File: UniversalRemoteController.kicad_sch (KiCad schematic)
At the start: 0 parts

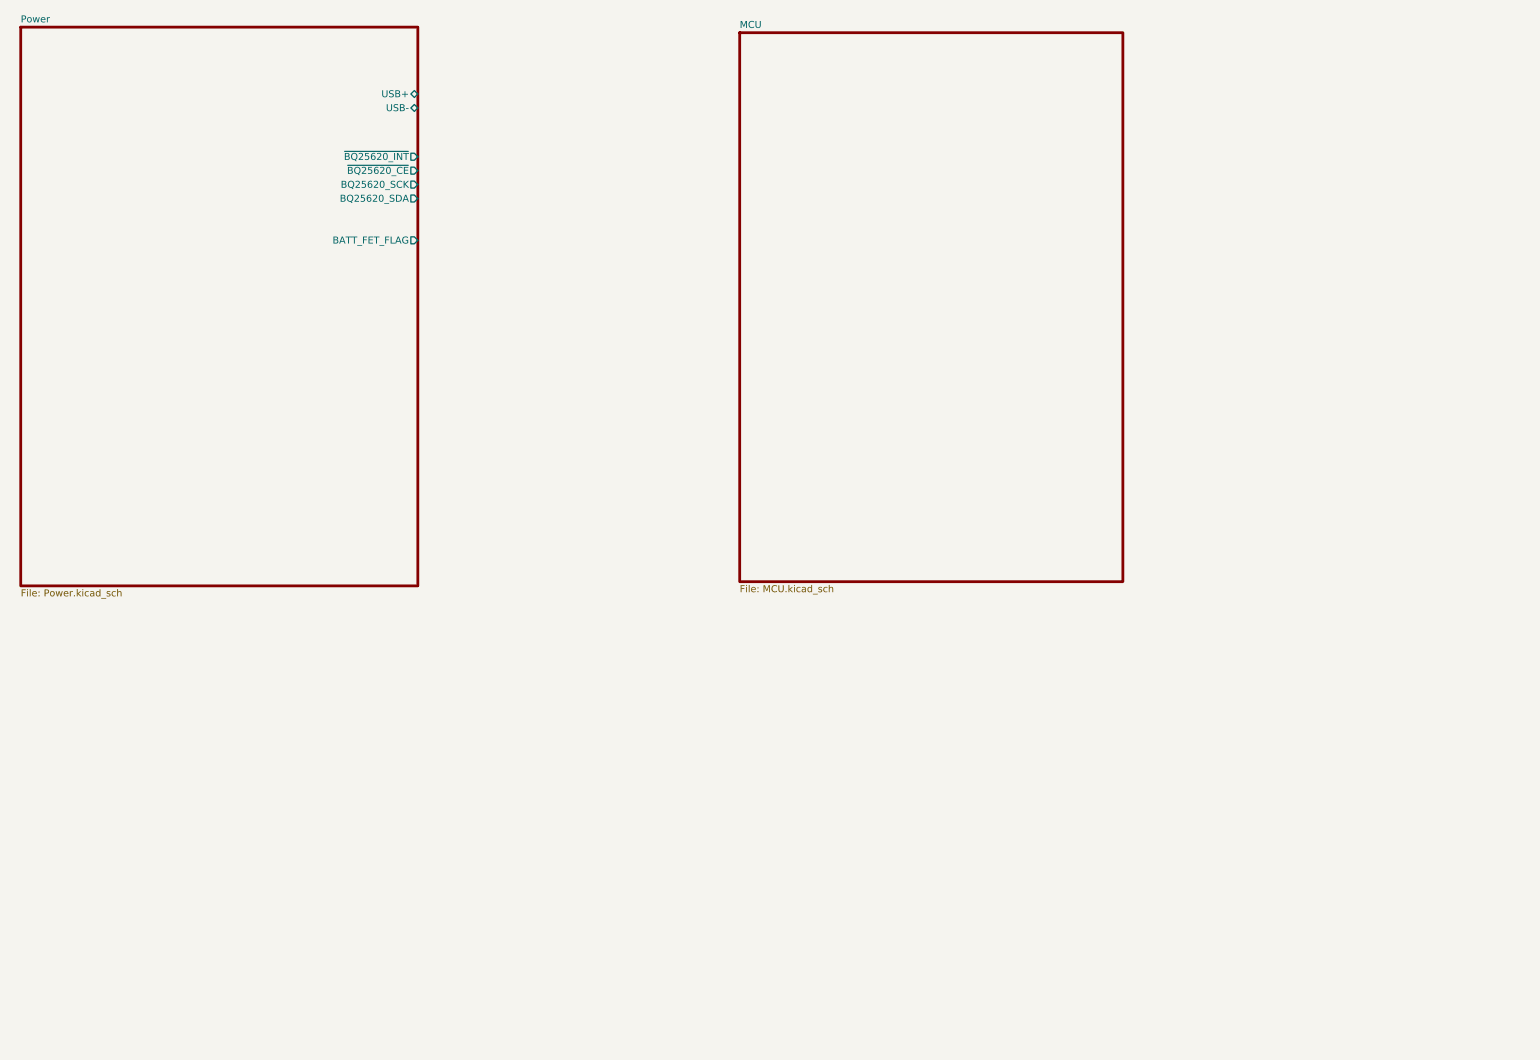
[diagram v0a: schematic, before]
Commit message: Add the SDRAM ic
16MB SDRAM add
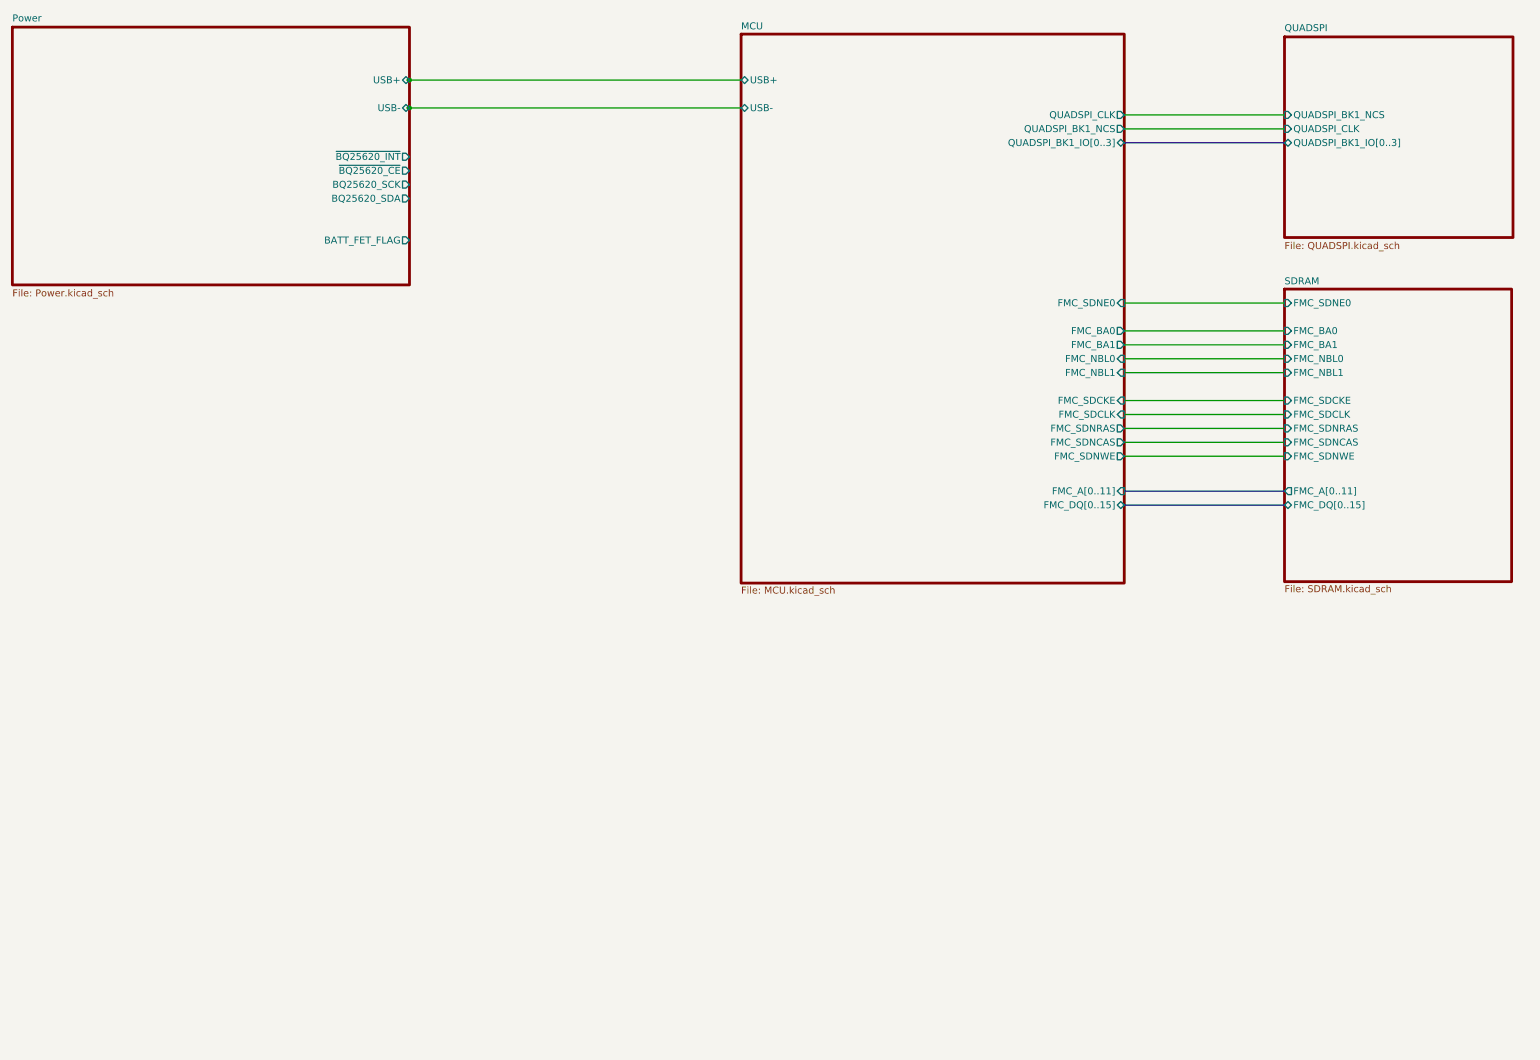
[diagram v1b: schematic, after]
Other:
- added sheet QUADSPI (QUADSPI.kicad_sch)
- added sheet SDRAM (SDRAM.kicad_sch)
- sheet MCU ports: added FMC_A[0..11], FMC_BA0, FMC_BA1, FMC_DQ[0..15], FMC_NBL0, FMC_NBL1, FMC_SDCKE, FMC_SDCLK, FMC_SDNCAS, FMC_SDNE0, FMC_SDNRAS, FMC_SDNWE, QUADSPI_BK1_IO[0..3], QUADSPI_BK1_NCS, QUADSPI_CLK, USB+, USB-; removed none

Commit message: Add the nrf and joystic module
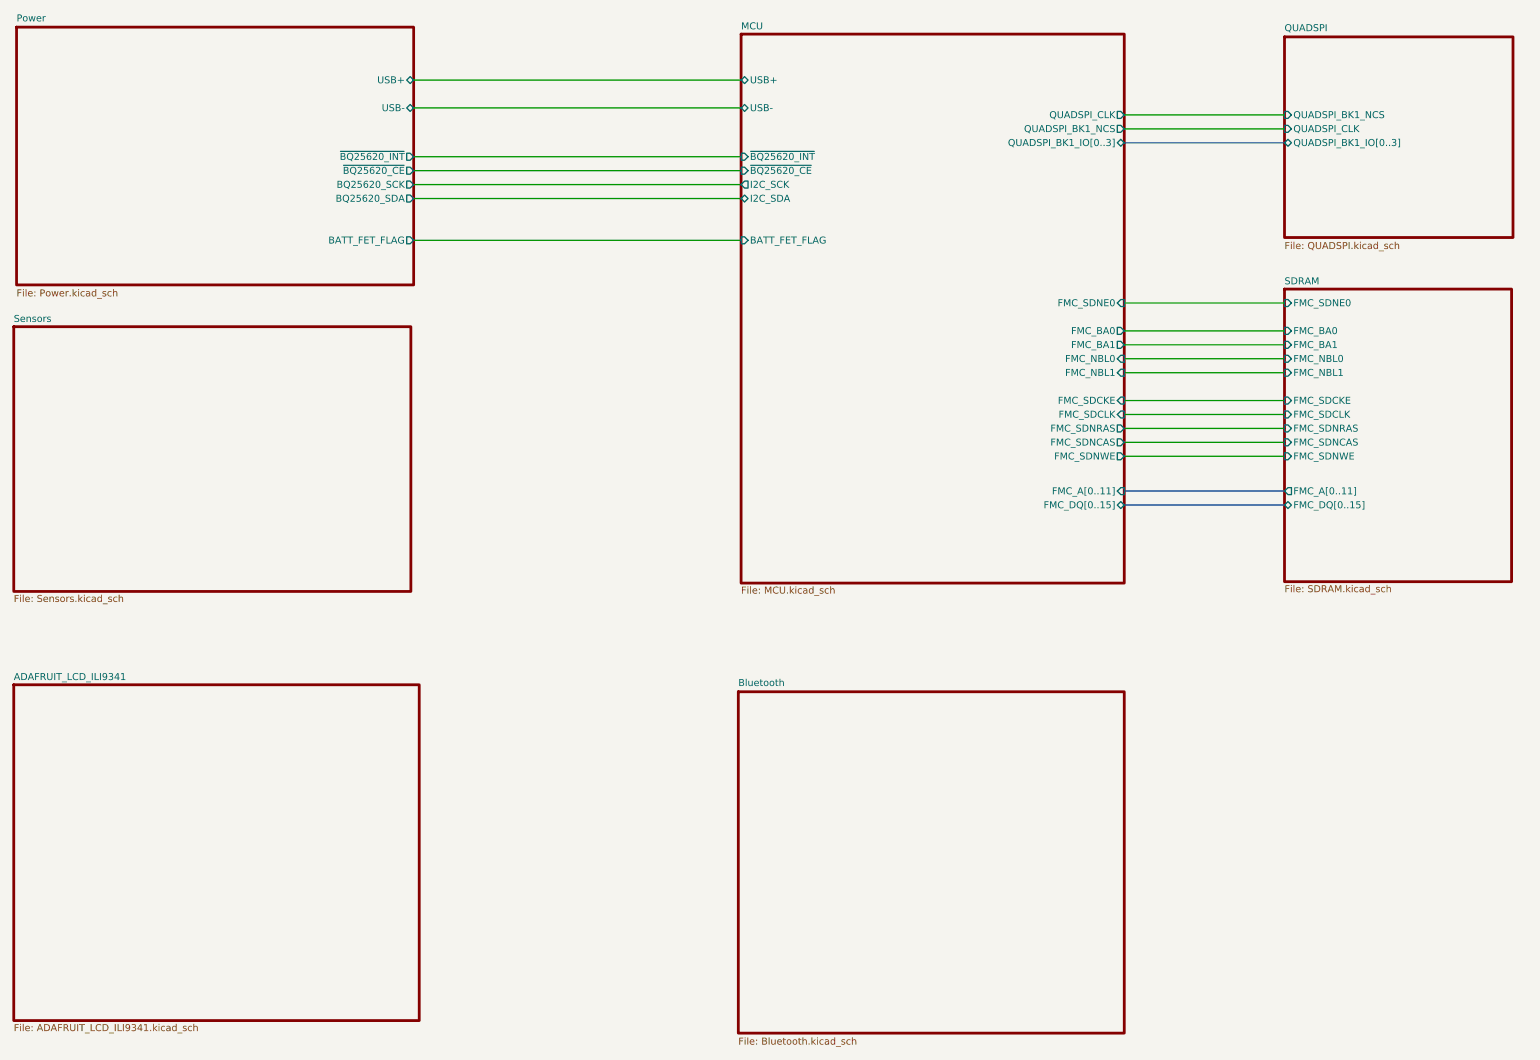
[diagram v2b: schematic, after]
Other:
- added sheet ADAFRUIT_LCD_ILI9341 (ADAFRUIT_LCD_ILI9341.kicad_sch)
- added sheet Bluetooth (Bluetooth.kicad_sch)
- added sheet Sensors (Sensors.kicad_sch)
- sheet MCU ports: added BATT_FET_FLAG, I2C_SCK, I2C_SDA, ~{BQ25620_CE}, ~{BQ25620_INT}; removed none
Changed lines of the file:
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@@
 		(rev "1.0")
 	)
-	(junction
-		(at 124.968 48.26)
-		(diameter 0)
-		(color 0 0 0 0)
-	)
-	(junction
-		(at 124.968 43.18)
-		(diameter 0)
-		(color 0 0 0 0)
+	(wire
+		(pts
+			(xy 125.73 72.39) (xy 185.42 72.39)
+		)
+		(stroke
+			(width 0)
+			(type default)
+		)
 	)
 	(wire
@@
 	(wire
 		(pts
-			(xy 124.968 48.26) (xy 185.42 48.26)
+			(xy 125.73 48.26) (xy 185.42 48.26)
 		)
 		(stroke
@@
 	(wire
 		(pts
-			(xy 124.968 43.18) (xy 185.42 43.18)
+			(xy 125.73 62.23) (xy 185.42 62.23)
+		)
+		(stroke
+			(width 0)
+			(type default)
+		)
+	)
+	(wire
+		(pts
+			(xy 125.73 43.18) (xy 185.42 43.18)
 		)
 		(stroke
@@
 	(wire
 		(pts
+			(xy 125.73 64.77) (xy 185.42 64.77)
+		)
+		(stroke
+			(width 0)
+			(type default)
+		)
+	)
+	(wire
+		(pts
 			(xy 255.27 109.22) (xy 284.48 109.22)
 		)
@@
 		)
 	)
-	(wire
-		(pts
-			(xy 124.46 43.18) (xy 124.968 43.18)
-		)
-		(stroke
-			(width 0)
-			(type default)
-		)
-	)
-	(wire
-		(pts
-			(xy 124.46 48.26) (xy 124.968 48.26)
-		)
-		(stroke
-			(width 0)
-			(type default)
-		)
-	)
 	(bus
 		(pts
@@
 	(wire
 		(pts
+			(xy 125.73 59.69) (xy 185.42 59.69)
+		)
+		(stroke
+			(width 0)
+			(type default)
+		)
+	)
+	(wire
+		(pts
 			(xy 255.27 106.68) (xy 284.48 106.68)
 		)
@@
 		(pts
 			(xy 255.27 111.76) (xy 284.48 111.76)
+		)
+		(stroke
+			(width 0)
+			(type default)
+		)
+	)
+	(wire
+		(pts
+			(xy 125.73 57.15) (xy 185.42 57.15)
 		)
 		(stroke
@@
 	)
 	(sheet
+		(at 52.832 153.416)
+		(size 73.914 61.214)
+		(fields_autoplaced yes)
+		(stroke
+			(width 0.508)
+			(type solid)
+			(color 255 163 155 1)
+		)
+		(fill
+			(color 254 255 106 1.0000)
+		)
+		(property "Sheetname" "ADAFRUIT_LCD_ILI9341"
+			(at 52.832 152.7044 0)
+			(effects
+				(font
+					(size 1.27 1.27)
+				)
+				(justify left bottom)
+			)
+		)
+		(property "Sheetfile" "ADAFRUIT_LCD_ILI9341.kicad_sch"
+			(at 52.832 215.2146 0)
+			(effects
+				(font
+					(size 1.27 1.27)
+				)
+				(justify left top)
+			)
+		)
+		(instances
+			(project "UniversalRemoteController"
+				(path "/dfe540b7-7587-4b82-94ea-0a8290455e48"
+					(page "7")
+				)
+			)
+		)
+	)
+	(sheet
 		(at 185.42 34.798)
 		(size 69.85 100.076)
@@
 				)
 				(justify right)
+			)
+		)
+		(pin "I2C_SCK" output
+			(at 185.42 62.23 180)
+			(effects
+				(font
+					(size 1.27 1.27)
+				)
+				(justify left)
+			)
+		)
+		(pin "I2C_SDA" bidirectional
+			(at 185.42 64.77 180)
+			(effects
+				(font
+					(size 1.27 1.27)
+				)
+				(justify left)
+			)
+		)
+		(pin "~{BQ25620_INT}" input
+			(at 185.42 57.15 180)
+			(effects
+				(font
+					(size 1.27 1.27)
+				)
+				(justify left)
+			)
+		)
+		(pin "BATT_FET_FLAG" input
+			(at 185.42 72.39 180)
+			(effects
+				(font
+					(size 1.27 1.27)
+				)
+				(justify left)
+			)
+		)
+		(pin "~{BQ25620_CE}" input
+			(at 185.42 59.69 180)
+			(effects
+				(font
+					(size 1.27 1.27)
+				)
+				(justify left)
 			)
 		)
@@
 	)
 	(sheet
-		(at 52.578 33.528)
-		(size 72.39 46.99)
+		(at 52.832 88.138)
+		(size 72.39 48.26)
 		(fields_autoplaced yes)
 		(stroke
@@
 			(color 254 255 106 1.0000)
 		)
+		(property "Sheetname" "Sensors"
+			(at 52.832 87.4264 0)
+			(effects
+				(font
+					(size 1.27 1.27)
+				)
+				(justify left bottom)
+			)
+		)
+		(property "Sheetfile" "Sensors.kicad_sch"
+			(at 52.832 136.9826 0)
+			(effects
+				(font
+					(size 1.27 1.27)
+				)
+				(justify left top)
+			)
+		)
+		(instances
+			(project "UniversalRemoteController"
+				(path "/dfe540b7-7587-4b82-94ea-0a8290455e48"
+					(page "6")
+				)
+			)
+		)
+	)
+	(sheet
+		(at 53.34 33.528)
+		(size 72.39 46.99)
+		(fields_autoplaced yes)
+		(stroke
+			(width 0.508)
+			(type solid)
+			(color 255 163 155 1)
+		)
+		(fill
+			(color 254 255 106 1.0000)
+		)
 		(property "Sheetname" "Power"
-			(at 52.578 32.6386 0)
+			(at 53.34 32.6386 0)
 			(effects
 				(font
@@
 		)
 		(property "Sheetfile" "Power.kicad_sch"
-			(at 52.578 81.2804 0)
+			(at 53.34 81.2804 0)
 			(effects
 				(font
@@
 		)
 		(pin "USB-" bidirectional
-			(at 124.968 48.26 0)
+			(at 125.73 48.26 0)
 			(effects
 				(font
@@
 		)
 		(pin "~{BQ25620_INT}" output
-			(at 124.968 57.15 0)
+			(at 125.73 57.15 0)
 			(effects
 				(font
@@
 		)
 		(pin "BQ25620_SCK" output
-			(at 124.968 62.23 0)
+			(at 125.73 62.23 0)
 			(effects
 				(font
@@
 		)
 		(pin "~{BQ25620_CE}" output
-			(at 124.968 59.69 0)
+			(at 125.73 59.69 0)
 			(effects
 				(font
@@
 		)
 		(pin "BQ25620_SDA" output
-			(at 124.968 64.77 0)
+			(at 125.73 64.77 0)
 			(effects
 				(font
@@
 		)
 		(pin "BATT_FET_FLAG" output
-			(at 124.968 72.39 0)
+			(at 125.73 72.39 0)
 			(effects
 				(font
@@
 		)
 		(pin "USB+" bidirectional
-			(at 124.968 43.18 0)
+			(at 125.73 43.18 0)
 			(effects
 				(font
@@
 				)
 			)
+		)
+	)
+	(sheet
+		(at 184.912 154.686)
+		(size 70.358 62.23)
+		(fields_autoplaced yes)
+		(stroke
+			(width 0.508)
+			(type solid)
+			(color 255 163 155 1)
+		)
+		(fill
+			(color 254 255 106 1.0000)
+		)
+		(property "Sheetname" "Bluetooth"
+			(at 184.912 153.7966 0)
+			(effects
+				(font
+					(size 1.27 1.27)
+				)
+				(justify left bottom)
+			)
+		)
+		(property "Sheetfile" "Bluetooth.kicad_sch"
+			(at 184.912 217.6784 0)
+			(effects
+				(font
+					(size 1.27 1.27)
+				)
+				(justify left top)
+			)
+		)
+		(instances
+			(project "UniversalRemoteController"
+				(path "/dfe540b7-7587-4b82-94ea-0a8290455e48"
+					(page "8")
+				)
+			)

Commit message: commit a sound version
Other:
- sheet Bluetooth renamed BluetoothWiFi
- added sheet Audio (audio.kicad_sch)
- sheet ADAFRUIT_LCD_ILI9341 ports: added ILI9341_LCD; removed none
- sheet BluetoothWiFi: file Bluetooth.kicad_sch -> BluetoothWifi.kicad_sch
- sheet BluetoothWiFi ports: added ESP32_EN, ESP32_RX, ESP32_TX; removed none
- sheet MCU ports: added AXL_SPI, BME280_I2C, ESP32_EN, ESP32_RX, ESP32_TX, ILI9341_LCD, JOY_LEFT_BUTTON, JOY_LEFT_H_ANALOG, JOY_LEFT_V_ANALOG, JOY_RIGHT_BUTTON, JOY_RIGHT_H_ANALOG, JOY_RIGHT_V_ANALOG, MIC_I2S; removed none
- sheet Sensors ports: added AXL_SPI, BME280_I2C, JOY_LEFT_BUTTON, JOY_LEFT_H_ANALOG, JOY_LEFT_V_ANALOG, JOY_RIGHT_BUTTON, JOY_RIGHT_H_ANALOG, JOY_RIGHT_V_ANALOG, MIC_I2S; removed none

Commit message: started the layout
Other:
- sheet Audio ports: added AUDIO_I2S; removed none
- sheet MCU ports: added AUDIO_I2S; removed MIC_I2S
- sheet Sensors ports: added AUDIO_I2S; removed MIC_I2S
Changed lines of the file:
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@@
 		(color 0 0 0 0)
 	)
+	(junction
+		(at 157.48 129.286)
+		(diameter 0)
+		(color 0 0 0 0)
+	)
 	(wire
 		(pts
@@
 		)
 	)
+	(bus
+		(pts
+			(xy 157.48 129.286) (xy 185.42 129.286)
+		)
+		(stroke
+			(width 0)
+			(type default)
+		)
+	)
 	(wire
 		(pts
@@
 		)
 	)
+	(bus
+		(pts
+			(xy 126.238 129.286) (xy 157.48 129.286)
+		)
+		(stroke
+			(width 0)
+			(type default)
+		)
+	)
 	(wire
 		(pts
@@
 		)
 	)
+	(bus
+		(pts
+			(xy 157.48 157.48) (xy 126.238 157.48)
+		)
+		(stroke
+			(width 0)
+			(type default)
+		)
+	)
 	(wire
 		(pts
@@
 		)
 	)
+	(bus
+		(pts
+			(xy 157.48 129.286) (xy 157.48 157.48)
+		)
+		(stroke
+			(width 0)
+			(type default)
+		)
+	)
 	(wire
 		(pts
@@
 		(pts
 			(xy 125.73 57.15) (xy 185.42 57.15)
-		)
-		(stroke
-			(width 0)
-			(type default)
-		)
-	)
-	(bus
-		(pts
-			(xy 125.73 113.03) (xy 185.42 113.03)
 		)
 		(stroke
@@
 			)
 		)
-		(pin "MIC_I2S" bidirectional
-			(at 185.42 113.03 180)
-			(effects
-				(font
-					(size 1.27 1.27)
-				)
-				(justify left)
-			)
-		)
 		(pin "BME280_I2C" bidirectional
 			(at 185.42 120.65 180)
+			(effects
+				(font
+					(size 1.27 1.27)
+				)
+				(justify left)
+			)
+		)
+		(pin "AUDIO_I2S" bidirectional
+			(at 185.42 129.286 180)
 			(effects
 				(font
@@
 			)
 		)
-		(pin "MIC_I2S" bidirectional
-			(at 126.238 113.03 0)
-			(effects
-				(font
-					(size 1.27 1.27)
-				)
-				(justify right)
-			)
-		)
 		(pin "AXL_SPI" bidirectional
 			(at 126.238 116.84 0)
+			(effects
+				(font
+					(size 1.27 1.27)
+				)
+				(justify right)
+			)
+		)
+		(pin "AUDIO_I2S" bidirectional
+			(at 126.238 129.286 0)
 			(effects
 				(font
@@
 			)
 		)
+		(pin "AUDIO_I2S" bidirectional
+			(at 126.238 157.48 0)
+			(effects
+				(font
+					(size 1.27 1.27)
+				)
+				(justify right)
+			)
+		)
